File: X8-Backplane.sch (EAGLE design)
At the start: 16 parts

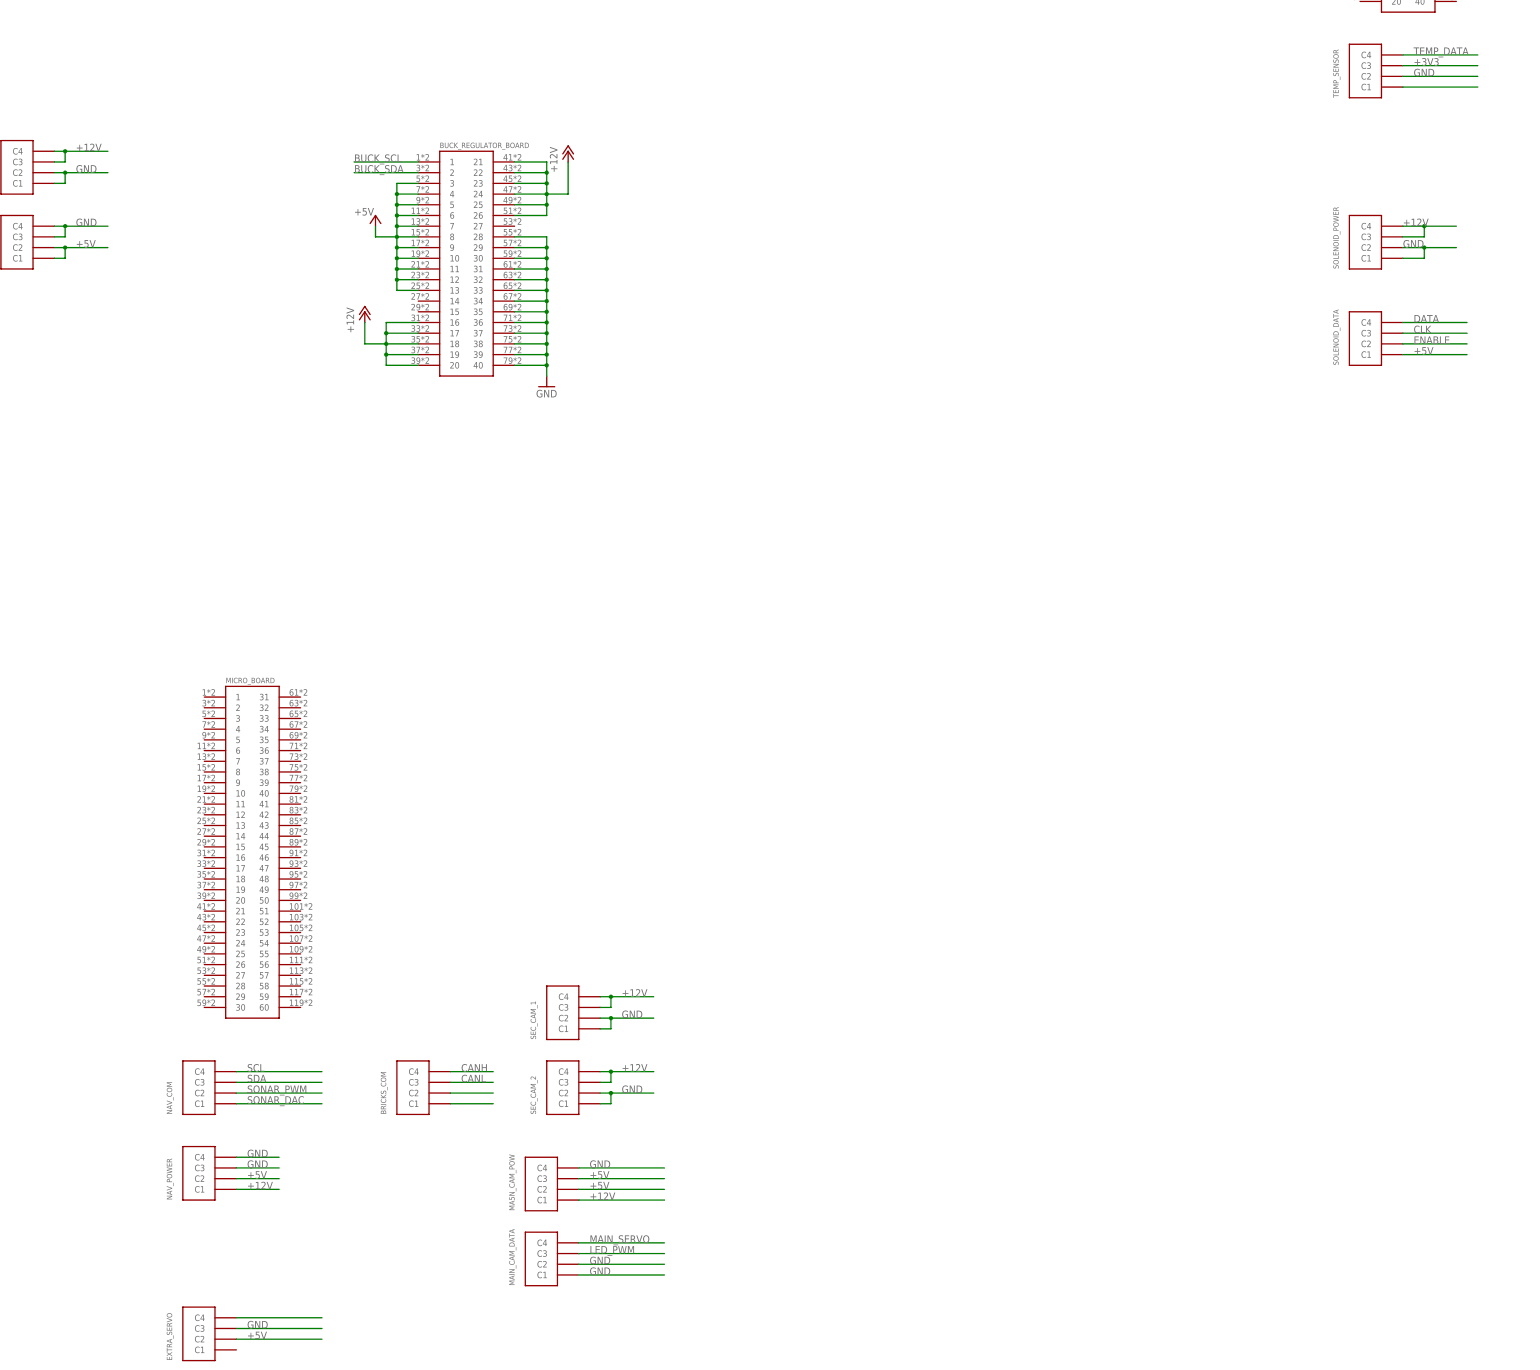
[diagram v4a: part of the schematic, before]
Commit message: Routed connections from micro board
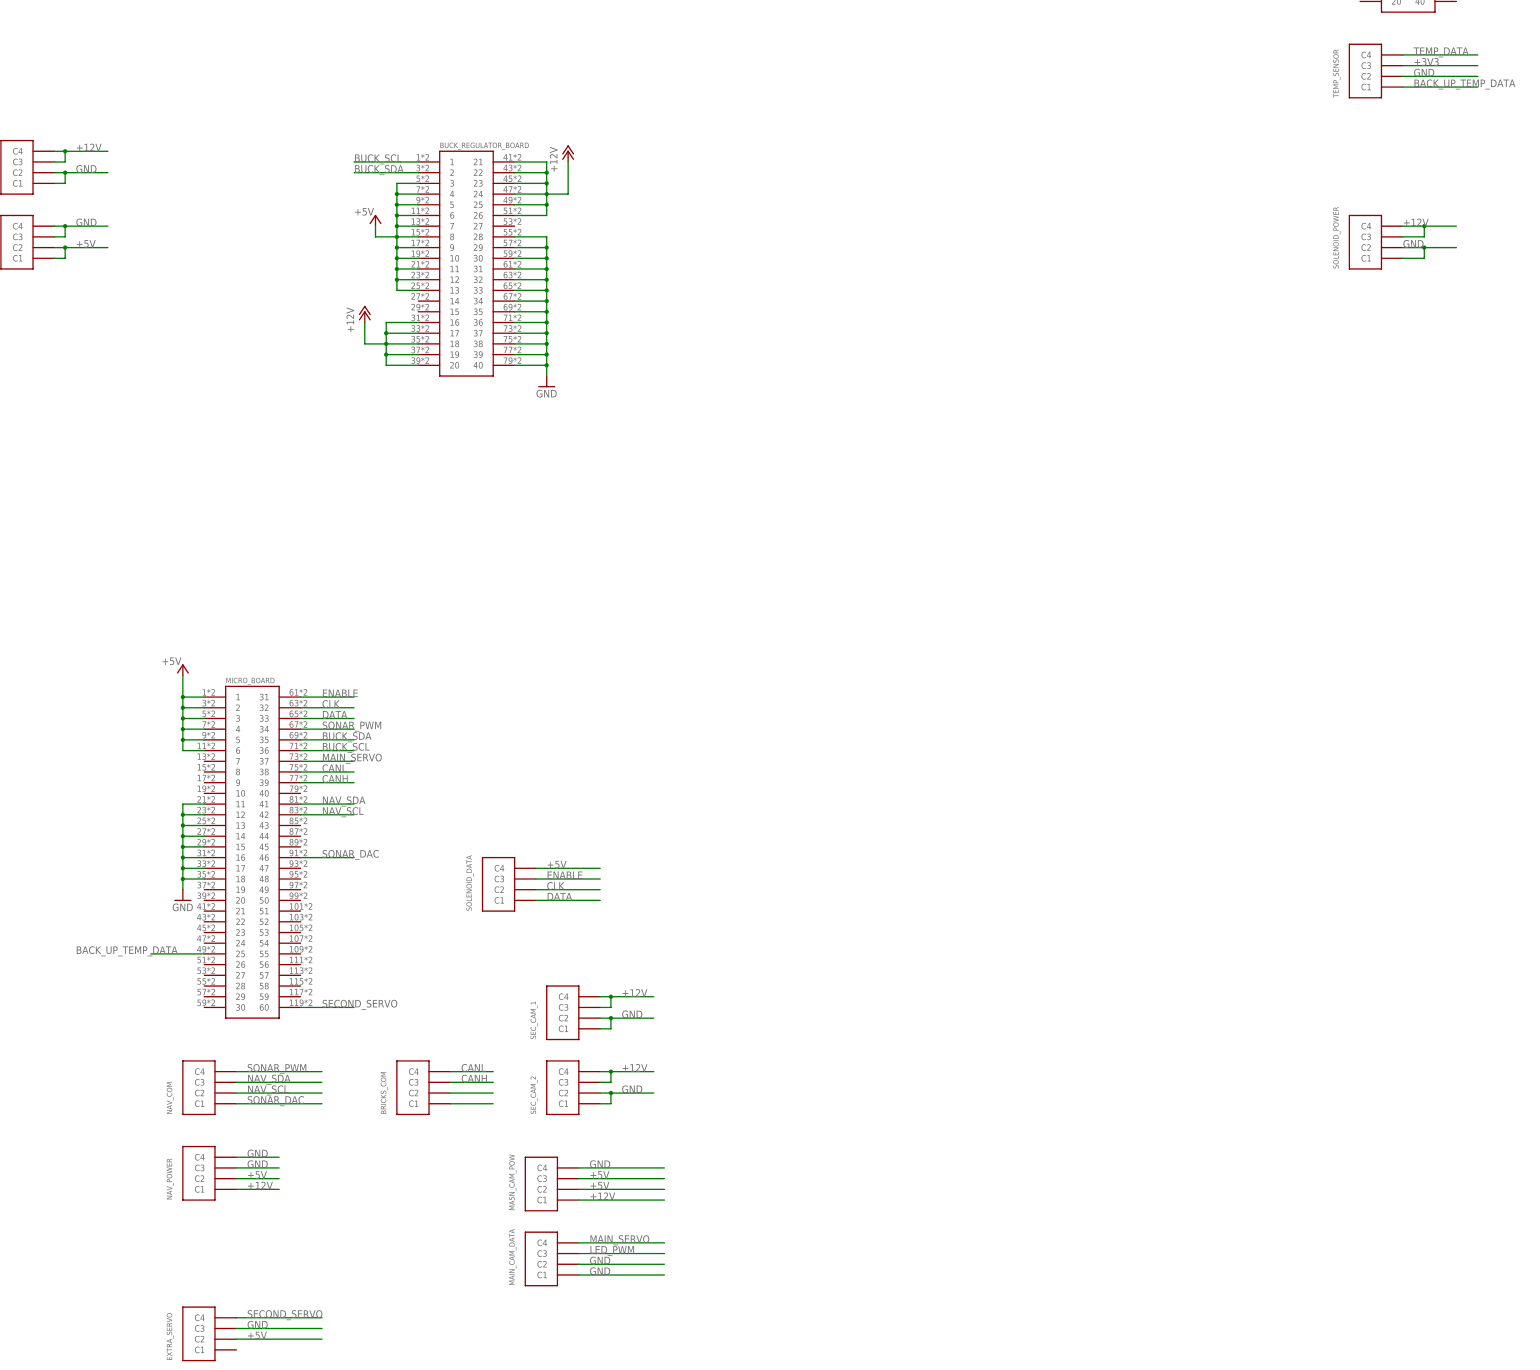
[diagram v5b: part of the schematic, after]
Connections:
- removed net N$7: TEMP_SENSOR.C1
- removed net SCL: NAV_COM.C4
- removed net SDA: NAV_COM.C3
- new net BACK_UP_TEMP_DATA: MICRO_BOARD.25, TEMP_SENSOR.C1
- new net NAV_SCL: MICRO_BOARD.42, NAV_COM.C2
- new net NAV_SDA: MICRO_BOARD.41, NAV_COM.C3
- net +5V: now also MICRO_BOARD.1, MICRO_BOARD.2, MICRO_BOARD.3, MICRO_BOARD.4, MICRO_BOARD.5, MICRO_BOARD.6, SOLENOID_DATA.C4; no longer SOLENOID_DATA.C1
- net BUCK_SCL: now also MICRO_BOARD.36
- net BUCK_SDA: now also MICRO_BOARD.35
- net CANH: now also BRICKS_COM.C3, MICRO_BOARD.39; no longer BRICKS_COM.C4
- net CANL: now also BRICKS_COM.C4, MICRO_BOARD.38; no longer BRICKS_COM.C3
- net CLK: now also MICRO_BOARD.32, SOLENOID_DATA.C2; no longer SOLENOID_DATA.C3
- net DATA: now also MICRO_BOARD.33, SOLENOID_DATA.C1; no longer SOLENOID_DATA.C4
- net ENABLE: now also MICRO_BOARD.31, SOLENOID_DATA.C3; no longer SOLENOID_DATA.C2
- net GND: now also MICRO_BOARD.11, MICRO_BOARD.12, MICRO_BOARD.13, MICRO_BOARD.14, MICRO_BOARD.15, MICRO_BOARD.16, MICRO_BOARD.17, MICRO_BOARD.18
- net MAIN_SERVO: now also MICRO_BOARD.37
- net SECOND_SERVO: now also MICRO_BOARD.60
- net SONAR_DAC: now also MICRO_BOARD.46
- net SONAR_PWM: now also MICRO_BOARD.34, NAV_COM.C4; no longer NAV_COM.C2
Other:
- moved on the sheet: SOLENOID_DATA

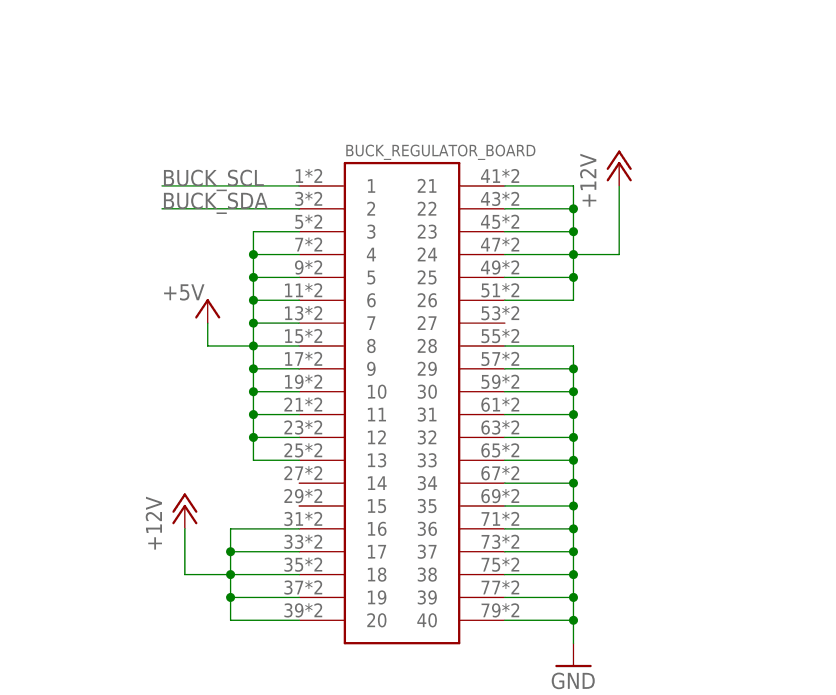
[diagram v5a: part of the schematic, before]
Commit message: Changed around the order of the connectors
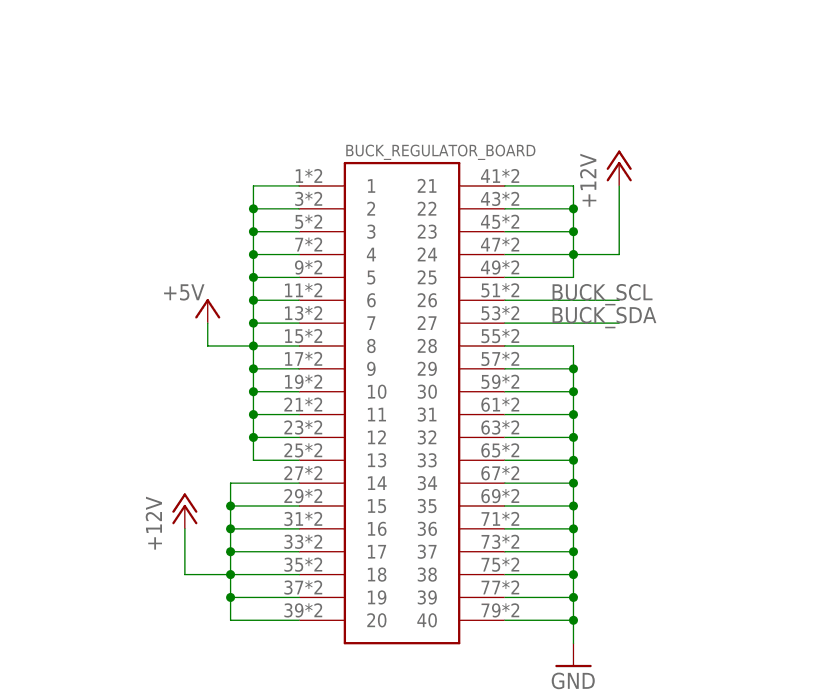
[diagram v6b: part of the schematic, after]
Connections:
- net +12V: now also BUCK_REGULATOR_BOARD.14, BUCK_REGULATOR_BOARD.15; no longer BUCK_REGULATOR_BOARD.26
- net +5V: now also BUCK_REGULATOR_BOARD.1, BUCK_REGULATOR_BOARD.2
- net BUCK_SCL: now also BUCK_REGULATOR_BOARD.26; no longer BUCK_REGULATOR_BOARD.1
- net BUCK_SDA: now also BUCK_REGULATOR_BOARD.27; no longer BUCK_REGULATOR_BOARD.2
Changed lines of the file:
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@@
 <wire x1="111.76" y1="68.58" x2="106.68" y2="68.58" width="0.1524" layer="91"/>
 <wire x1="106.68" y1="68.58" x2="106.68" y2="73.66" width="0.1524" layer="91"/>
+<wire x1="111.76" y1="73.66" x2="111.76" y2="76.2" width="0.1524" layer="91"/>
+<junction x="111.76" y="73.66"/>
+<pinref part="BUCK_REGULATOR_BOARD" gate="G$1" pin="15"/>
+<wire x1="111.76" y1="76.2" x2="119.38" y2="76.2" width="0.1524" layer="91"/>
+<wire x1="111.76" y1="76.2" x2="111.76" y2="78.74" width="0.1524" layer="91"/>
+<junction x="111.76" y="76.2"/>
+<pinref part="BUCK_REGULATOR_BOARD" gate="G$1" pin="14"/>
+<wire x1="111.76" y1="78.74" x2="119.38" y2="78.74" width="0.1524" layer="91"/>
 </segment>
 <segment>
@@
 <wire x1="142.24" y1="111.76" x2="149.86" y2="111.76" width="0.1524" layer="91"/>
 <wire x1="149.86" y1="111.76" x2="149.86" y2="109.22" width="0.1524" layer="91"/>
-<pinref part="BUCK_REGULATOR_BOARD" gate="G$1" pin="26"/>
 <wire x1="149.86" y1="109.22" x2="149.86" y2="106.68" width="0.1524" layer="91"/>
 <wire x1="149.86" y1="106.68" x2="149.86" y2="104.14" width="0.1524" layer="91"/>
 <wire x1="149.86" y1="104.14" x2="149.86" y2="101.6" width="0.1524" layer="91"/>
-<wire x1="149.86" y1="101.6" x2="149.86" y2="99.06" width="0.1524" layer="91"/>
-<wire x1="149.86" y1="99.06" x2="142.24" y2="99.06" width="0.1524" layer="91"/>
 <pinref part="BUCK_REGULATOR_BOARD" gate="G$1" pin="25"/>
 <wire x1="142.24" y1="101.6" x2="149.86" y2="101.6" width="0.1524" layer="91"/>
-<junction x="149.86" y="101.6"/>
 <pinref part="BUCK_REGULATOR_BOARD" gate="G$1" pin="24"/>
 <wire x1="142.24" y1="104.14" x2="149.86" y2="104.14" width="0.1524" layer="91"/>
@@
 <wire x1="109.22" y1="93.98" x2="109.22" y2="96.52" width="0.1524" layer="91"/>
 <pinref part="P+5" gate="1" pin="+5V"/>
+<wire x1="114.3" y1="106.68" x2="114.3" y2="109.22" width="0.1524" layer="91"/>
+<junction x="114.3" y="106.68"/>
+<pinref part="BUCK_REGULATOR_BOARD" gate="G$1" pin="2"/>
+<wire x1="114.3" y1="109.22" x2="119.38" y2="109.22" width="0.1524" layer="91"/>
+<wire x1="114.3" y1="109.22" x2="114.3" y2="111.76" width="0.1524" layer="91"/>
+<junction x="114.3" y="109.22"/>
+<pinref part="BUCK_REGULATOR_BOARD" gate="G$1" pin="1"/>
+<wire x1="114.3" y1="111.76" x2="119.38" y2="111.76" width="0.1524" layer="91"/>
 </segment>
 <segment>
@@
 <net name="BUCK_SCL" class="0">
 <segment>
-<pinref part="BUCK_REGULATOR_BOARD" gate="G$1" pin="1"/>
-<wire x1="119.38" y1="111.76" x2="104.14" y2="111.76" width="0.1524" layer="91"/>
-<label x="104.14" y="111.76" size="1.778" layer="95"/>
-</segment>
-<segment>
 <pinref part="MICRO_BOARD" gate="G$1" pin="36"/>
 <wire x1="91.44" y1="-27.94" x2="104.14" y2="-27.94" width="0.1524" layer="91"/>
 <label x="96.52" y="-27.94" size="1.778" layer="95"/>
 </segment>
+<segment>
+<pinref part="BUCK_REGULATOR_BOARD" gate="G$1" pin="26"/>
+<wire x1="142.24" y1="99.06" x2="154.94" y2="99.06" width="0.1524" layer="91"/>
+<label x="147.32" y="99.06" size="1.778" layer="95"/>
+</segment>
 </net>
 <net name="BUCK_SDA" class="0">
-<segment>
-<pinref part="BUCK_REGULATOR_BOARD" gate="G$1" pin="2"/>
-<wire x1="119.38" y1="109.22" x2="104.14" y2="109.22" width="0.1524" layer="91"/>
-<label x="104.14" y="109.22" size="1.778" layer="95"/>
-</segment>
 <segment>
 <pinref part="MICRO_BOARD" gate="G$1" pin="35"/>
@@
 <label x="96.52" y="-25.4" size="1.778" layer="95"/>
 </segment>
-</net>
+<segment>
+<pinref part="BUCK_REGULATOR_BOARD" gate="G$1" pin="27"/>
+<wire x1="142.24" y1="96.52" x2="154.94" y2="96.52" width="0.1524" layer="91"/>
+<label x="147.32" y="96.52" size="1.778" layer="95"/>
+</segment>
+</net>

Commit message: Changed more connector lines
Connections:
- net BUCK_SCL: now also BUCK_REGULATOR_BOARD.27; no longer BUCK_REGULATOR_BOARD.26
- net BUCK_SDA: now also BUCK_REGULATOR_BOARD.26; no longer BUCK_REGULATOR_BOARD.27
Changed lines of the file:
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@@
 </segment>
 <segment>
-<pinref part="BUCK_REGULATOR_BOARD" gate="G$1" pin="26"/>
-<wire x1="142.24" y1="99.06" x2="154.94" y2="99.06" width="0.1524" layer="91"/>
-<label x="147.32" y="99.06" size="1.778" layer="95"/>
+<pinref part="BUCK_REGULATOR_BOARD" gate="G$1" pin="27"/>
+<wire x1="142.24" y1="96.52" x2="154.94" y2="96.52" width="0.1524" layer="91"/>
+<label x="147.32" y="96.52" size="1.778" layer="95"/>
 </segment>
 </net>
@@
 </segment>
 <segment>
-<pinref part="BUCK_REGULATOR_BOARD" gate="G$1" pin="27"/>
-<wire x1="142.24" y1="96.52" x2="154.94" y2="96.52" width="0.1524" layer="91"/>
-<label x="147.32" y="96.52" size="1.778" layer="95"/>
+<pinref part="BUCK_REGULATOR_BOARD" gate="G$1" pin="26"/>
+<wire x1="142.24" y1="99.06" x2="154.94" y2="99.06" width="0.1524" layer="91"/>
+<label x="147.32" y="99.06" size="1.778" layer="95"/>
 </segment>
 </net>

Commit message: Finished the backplane
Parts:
- renumbered MA5N_CAM_POW to MAIN_CAM_POW
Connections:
- net +12V: now also APPLICATION_BOARD.11, APPLICATION_BOARD.12, APPLICATION_BOARD.13, APPLICATION_BOARD.14, APPLICATION_BOARD.15, APPLICATION_BOARD.16, APPLICATION_BOARD.17, MAIN_CAM_POW.C4, NAV_POWER.C4, POWER_INPUT.C1, POWER_INPUT.C2, SEC_CAM_1.C1, SEC_CAM_1.C2, SEC_CAM_2.C1, SEC_CAM_2.C2, SOLENOID_POWER.C1, SOLENOID_POWER.C2; no longer MAIN_CAM_POW.C1, NAV_POWER.C1, POWER_INPUT.C3, POWER_INPUT.C4, SEC_CAM_1.C3, SEC_CAM_1.C4, SEC_CAM_2.C3, SEC_CAM_2.C4, SOLENOID_POWER.C3, SOLENOID_POWER.C4
- net +3V3: now also APPLICATION_BOARD.29
- net +5V: now also APPLICATION_BOARD.10, APPLICATION_BOARD.5, APPLICATION_BOARD.6, APPLICATION_BOARD.7, APPLICATION_BOARD.8, APPLICATION_BOARD.9, EXTRA_SERVO.C4, MAIN_CAM_DATA.C1, MAIN_CAM_DATA.C2, NAV_POWER.C1, SOLENOID_DATA.C1; no longer EXTRA_SERVO.C2, MAIN_CAM_POW.C2, MAIN_CAM_POW.C3, NAV_POWER.C2, SOLENOID_DATA.C4
- net CANH: now also APPLICATION_BOARD.35, BRICKS_COM.C4; no longer BRICKS_COM.C3
- net CANL: now also APPLICATION_BOARD.33, BRICKS_COM.C3; no longer BRICKS_COM.C4
- net CLK: now also SOLENOID_DATA.C3; no longer SOLENOID_DATA.C2
- net DATA: now also SOLENOID_DATA.C4; no longer SOLENOID_DATA.C1
- net ENABLE: now also SOLENOID_DATA.C2; no longer SOLENOID_DATA.C3
- net GND: now also APPLICATION_BOARD.19, APPLICATION_BOARD.20, APPLICATION_BOARD.21, APPLICATION_BOARD.22, APPLICATION_BOARD.23, APPLICATION_BOARD.24, APPLICATION_BOARD.25, APPLICATION_BOARD.26, MAIN_CAM_POW.C1, MAIN_CAM_POW.C2, MAIN_CAM_POW.C3, NAV_POWER.C2, POWER_INPUT.C3, POWER_INPUT.C4, SEC_CAM_1.C3, SEC_CAM_1.C4, SEC_CAM_2.C3, SEC_CAM_2.C4, SOLENOID_POWER.C3, SOLENOID_POWER.C4; no longer MAIN_CAM_DATA.C1, MAIN_CAM_DATA.C2, MAIN_CAM_POW.C4, NAV_POWER.C4, POWER_INPUT.C1, POWER_INPUT.C2, SEC_CAM_1.C1, SEC_CAM_1.C2, SEC_CAM_2.C1, SEC_CAM_2.C2, SOLENOID_POWER.C1, SOLENOID_POWER.C2
- net LED_PWM: now also APPLICATION_BOARD.1, APPLICATION_BOARD.2, APPLICATION_BOARD.3, APPLICATION_BOARD.4
- net SECOND_SERVO: now also EXTRA_SERVO.C2; no longer EXTRA_SERVO.C4
- net TEMP_DATA: now also APPLICATION_BOARD.30
